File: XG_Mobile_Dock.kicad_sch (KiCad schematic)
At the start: 24 parts, among them J1 5-1775443-8, J2 20455-040E-76, J3 20455-040E-76, J4 3-2362375-4, J7 Conn_02x10_Odd_Even, J8 Conn_02x10_Odd_Even

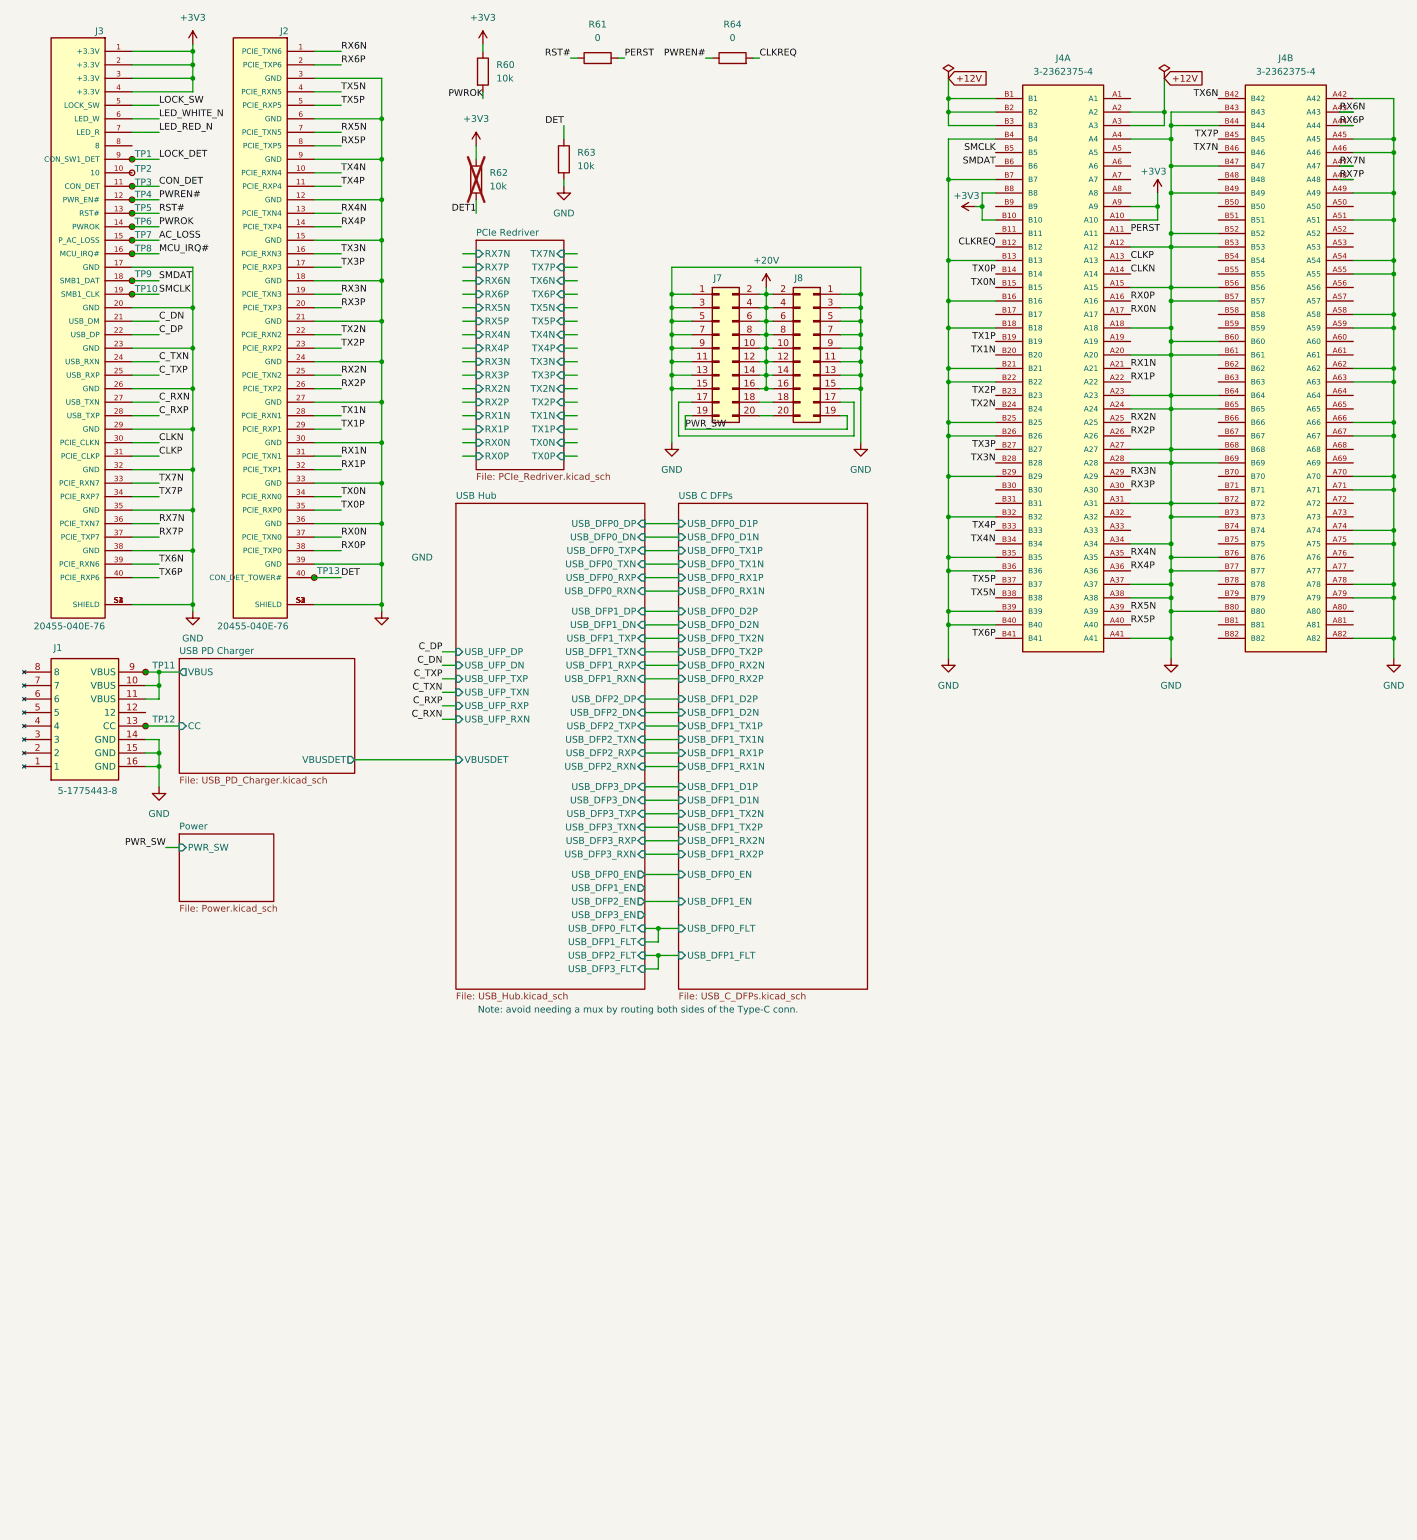
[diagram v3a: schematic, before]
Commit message: Added MCU
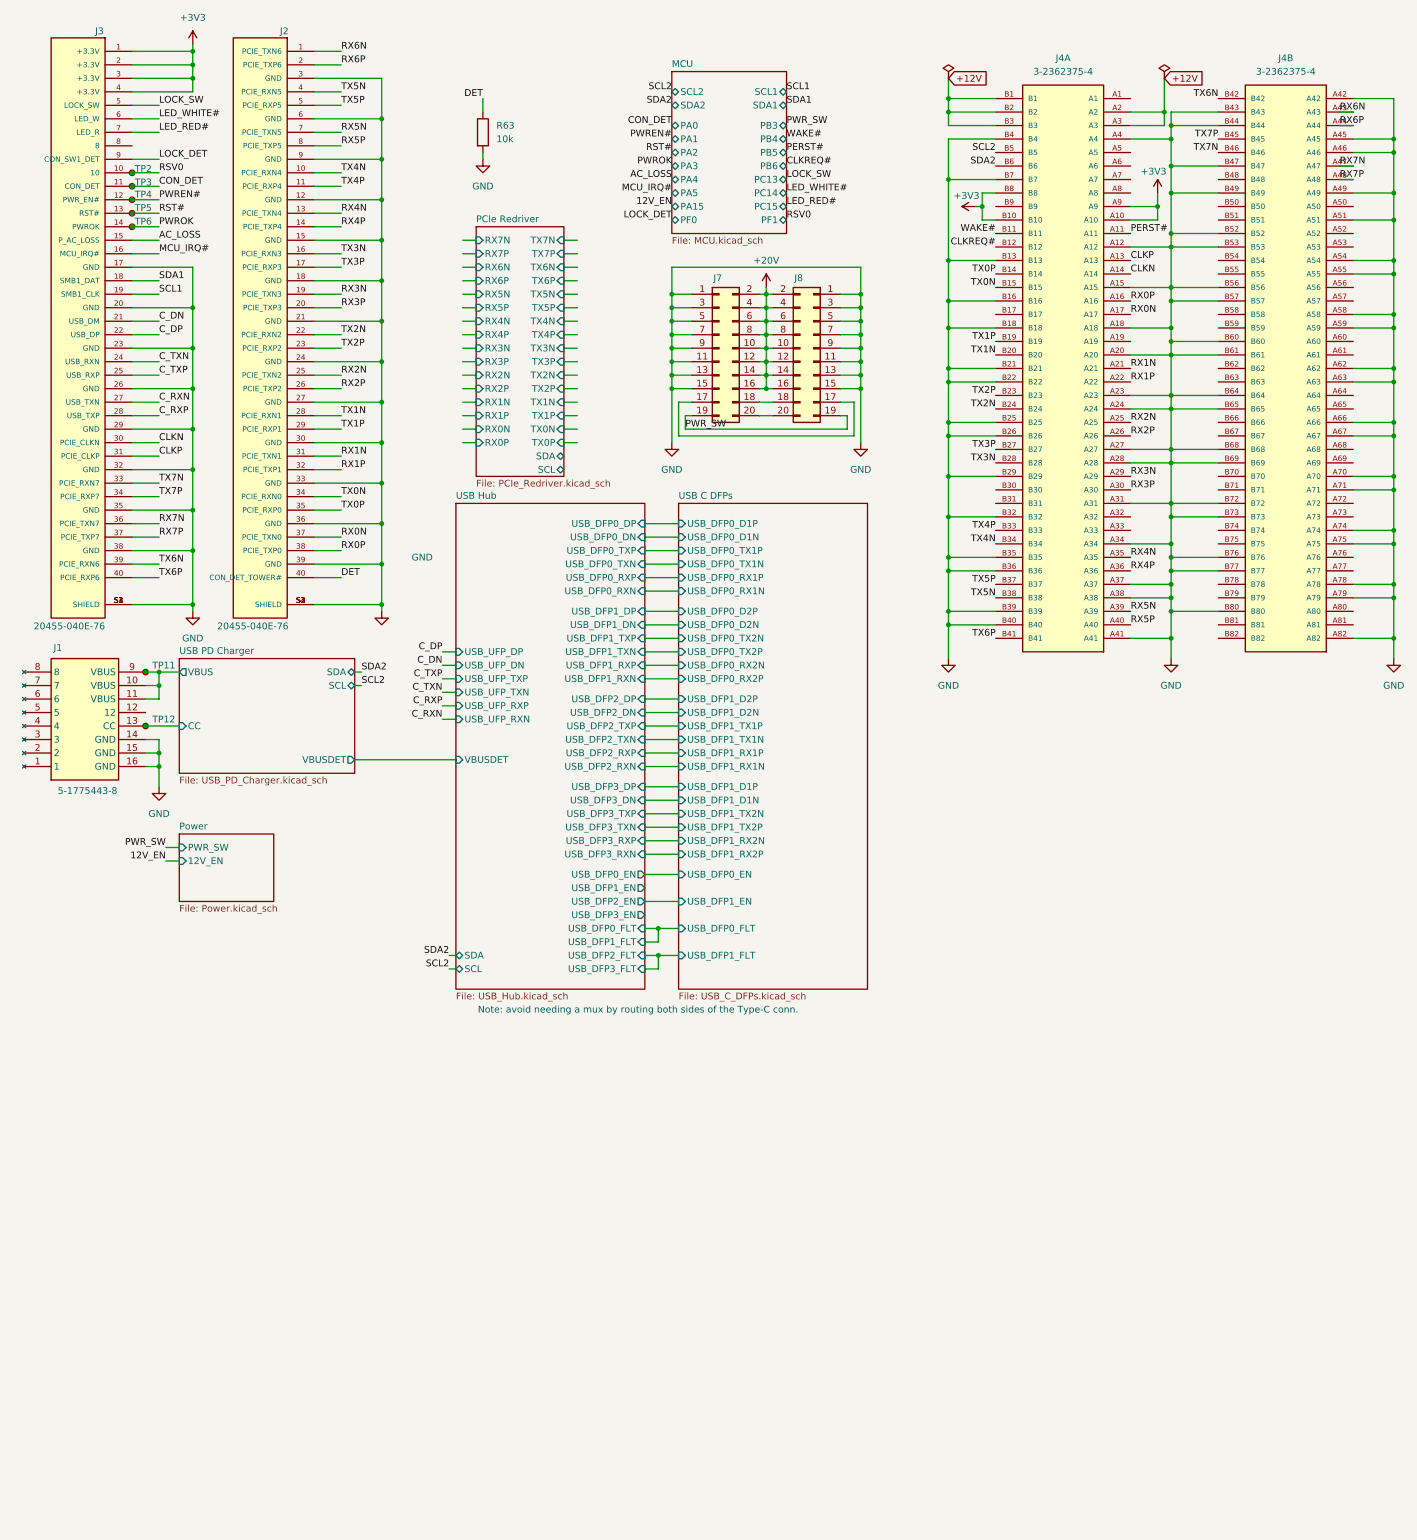
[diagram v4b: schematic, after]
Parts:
- removed R60, R62: 10k, Resistor_SMD:R_0402_1005Metric, symbol Device:R
- removed R61, R64: 0, Resistor_SMD:R_0805_2012Metric_Pad1.20x1.40mm_HandSolder, symbol Device:R
- removed TP1, TP10, TP13, TP7, TP8, TP9: TestPoint_Small, TestPoint:TestPoint_Pad_D1.0mm, symbol Connector:TestPoint_Small
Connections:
- net RSV0: now reaches J3.10, TP2.1
- net WAKE#: now reaches J4.B11
- net CLKREQ renamed CLKREQ#
- net LED_RED_N renamed LED_RED#
- net LED_WHITE_N renamed LED_WHITE#
- net PERST renamed PERST#
- net SMCLK renamed SCL1
- net SCL1: no longer J4.B5
- net SMDAT renamed SDA1
- net SDA1: no longer J4.B6
- new net SCL2: J4.B5
- new net SDA2: J4.B6
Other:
- added sheet MCU (MCU.kicad_sch)
- sheet PCIe Redriver ports: added SCL, SDA; removed none
- sheet Power ports: added 12V_EN; removed none
- sheet USB Hub ports: added SCL, SDA; removed none
- sheet USB PD Charger ports: added SCL, SDA; removed none
- moved on the sheet: R63

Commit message: Fixed all DRC errors
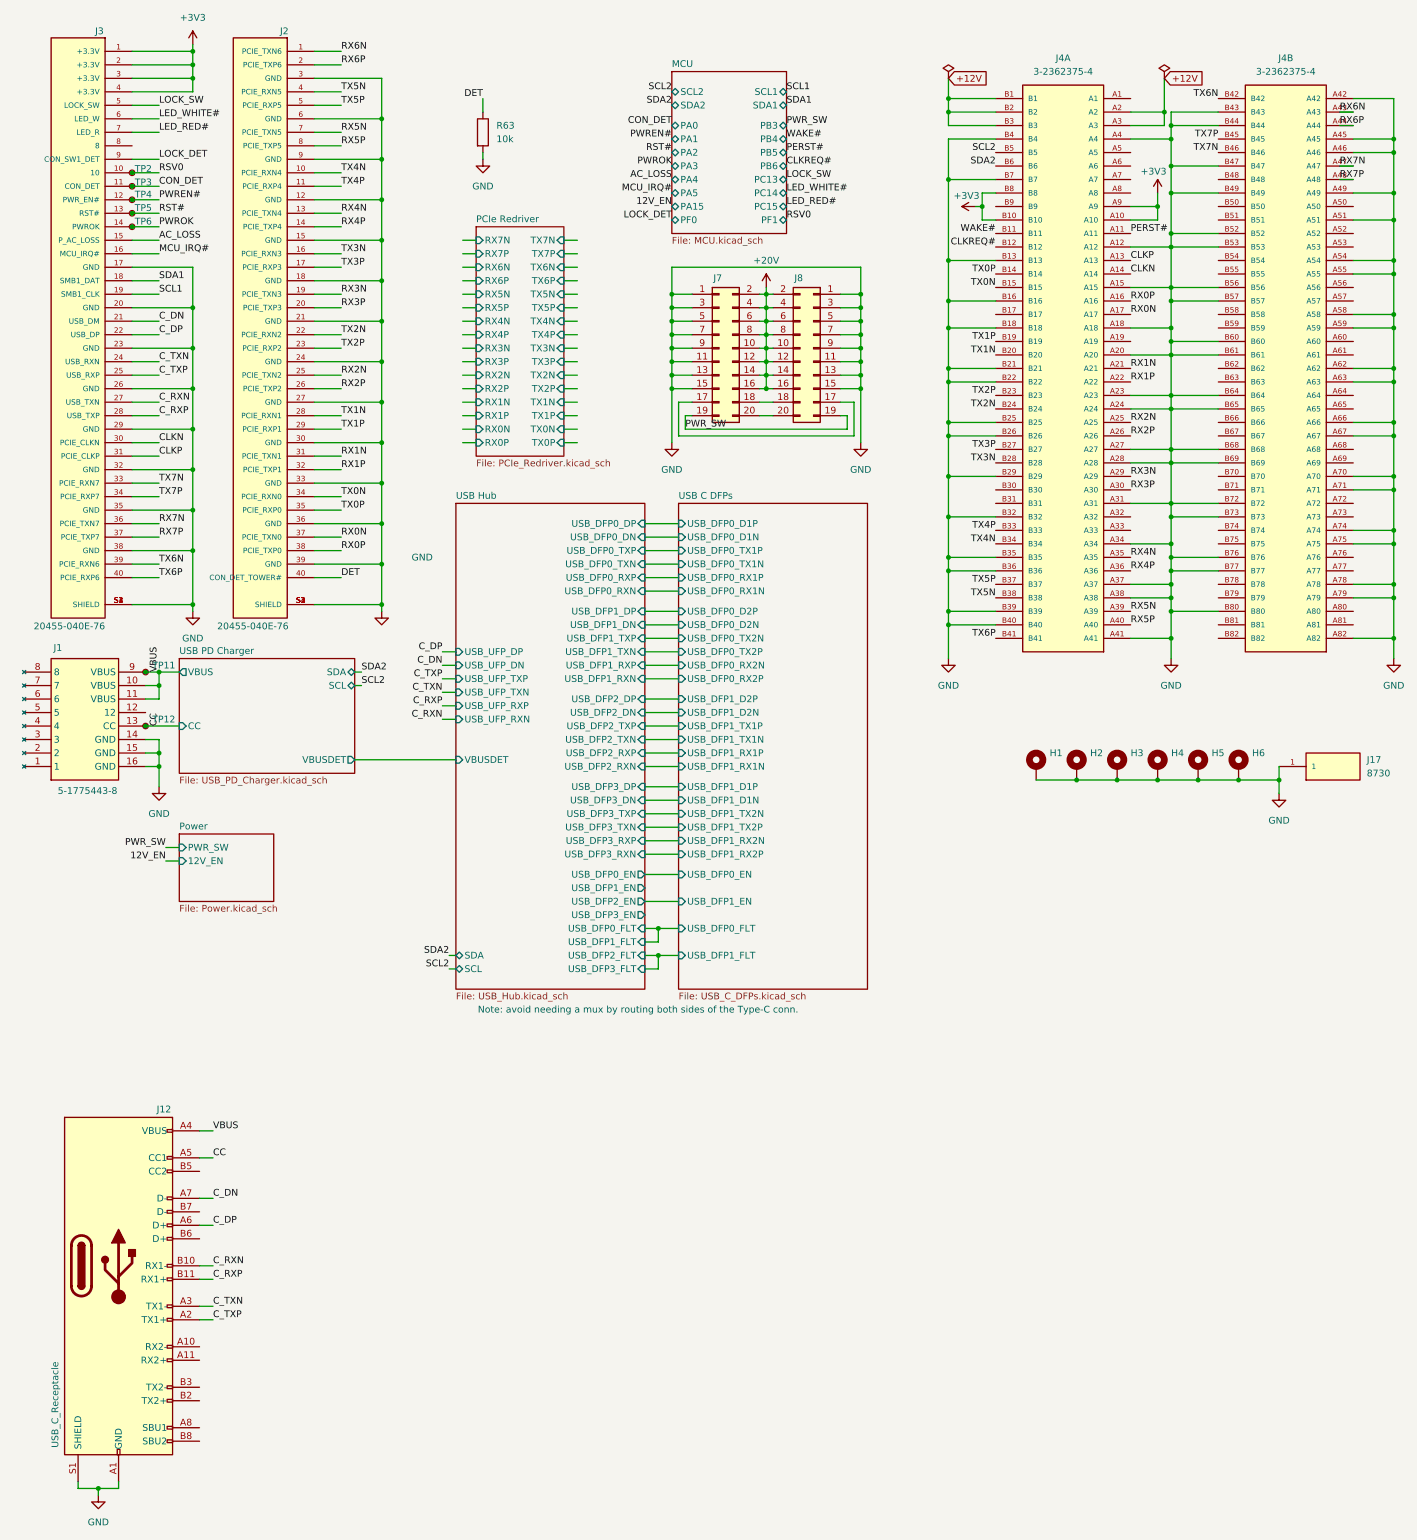
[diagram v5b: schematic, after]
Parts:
- added H1, H2, H3, H4, H5, H6: ~, XG_Mobile:Hole_200mil, symbol Mechanical:MountingHole_Pad
- added J12: USB_C_Receptacle, USB-C-SMD_TYPE-C-24P-QT:USB-C-SMD_TYPE-C-24P-QT, symbol Connector:USB_C_Receptacle
- added J17: 8730, KEYSTONE_8730:KEYSTONE_8730, symbol KEYSTONE_8730:8730
- J1: footprint 5-1775443-8 -> 5-1775443-8:5-1775443-8
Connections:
- net C_DN: now also J12.A7 (D-)
- net C_DP: now also J12.A6 (D+)
- net C_RXN: now also J12.B10 (RX1-)
- net C_RXP: now also J12.B11 (RX1+)
- net C_TXN: now also J12.A3 (TX1-)
- net C_TXP: now also J12.A2 (TX1+)
- net GND: now also H1.1, H2.1, H3.1, H4.1, H5.1, H6.1, J12.A1 (GND), J12.A12 (GND), J12.B1 (GND), J12.B12 (GND), J12.S1 (SHIELD), J17.1
- net USB PD Charger/CC renamed CC
- net CC: now also J12.A5 (CC1)
- net USB PD Charger/VBUS renamed VBUS
- net VBUS: now also J12.A4 (VBUS), J12.A9 (VBUS), J12.B4 (VBUS), J12.B9 (VBUS)
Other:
- sheet PCIe Redriver ports: added none; removed SCL, SDA
